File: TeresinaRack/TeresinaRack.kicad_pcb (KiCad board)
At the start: 12 copper layers, 68 x 40 mm, 209 parts, among them J3 USB_Micro-B, J4 SWD, J5 PATCH_SM_EDGE, Q1 MMBT3904, Q2 MMBT3904, SW1 RESET, SW2 BOOT, U1 STM32H750IBK6, U12 TL074, U13 MCP6004, U14 MCP6004, U15 MCP6004, U16 LM4040DBZ-10, U2 IS25LP064A, U3 AS4C16M32MSA-6BIN, U4 PCM3060, U6 TPS62170DSGR, U7 LD1117S50, U8 USBLC6-2SC6, Y1 16MHz

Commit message: Fix via-in-keepout and add bottom-side fiducials
- Move +3V3 edge-feed via (3.18,7.27) out of the F/B keepout zone
- Add FIDB2/FIDB3 (B.Cu) for double-sided assembly vision (3 bottom fiducials)
- U6 PG left unconnected by design (unused open-drain, no pull-up needed)
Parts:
- added FIDB2: Fiducial_1mm_Mask2mm, Fiducial_1mm_Mask2mm, B.Cu at (58.0, 30.4)
- added FIDB3: Fiducial_1mm_Mask2mm, Fiducial_1mm_Mask2mm, B.Cu at (49.9, 11.4)
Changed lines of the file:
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@@
 		)
 	)
+	(footprint "Fiducial_1mm_Mask2mm"
+		(layer "B.Cu")
+		(at 49.9 11.4 180)
+		(descr "Fiducial, circular marking, 1mm bare copper, 2mm soldermask opening (Level A)")
+		(tags "fiducial")
+		(property "Reference" "FIDB3"
+			(at 0 1.95 0)
+			(layer "B.SilkS")
+			(effects
+				(font
+					(size 1 1)
+					(thickness 0.15)
+				)
+				(justify mirror)
+			)
+		)
+		(property "Value" "Fiducial_1mm_Mask2mm"
+			(at 0 -1.95 0)
+			(layer "B.Fab")
+			(effects
+				(font
+					(size 1 1)
+					(thickness 0.15)
+				)
+				(justify mirror)
+			)
+		)
+		(property "Datasheet" ""
+			(at 0 0 0)
+			(layer "B.Fab")
+			(hide yes)
+			(effects
+				(font
+					(size 1.27 1.27)
+				)
+				(justify mirror)
+			)
+		)
+		(property "Description" ""
+			(at 0 0 0)
+			(layer "B.Fab")
+			(hide yes)
+			(effects
+				(font
+					(size 1.27 1.27)
+				)
+				(justify mirror)
+			)
+		)
+		(property "KiLib_Generator" "fiducial"
+			(at 0 0 0)
+			(layer "B.SilkS")
+			(hide yes)
+			(effects
+				(font
+					(size 1 1)
+					(thickness 0.15)
+				)
+				(justify mirror)
+			)
+		)
+		(attr smd exclude_from_pos_files exclude_from_bom)
+		(duplicate_pad_numbers_are_jumpers no)
+		(fp_circle
+			(center 0 0)
+			(end 1.25 0)
+			(stroke
+				(width 0.05)
+				(type solid)
+			)
+			(fill no)
+			(layer "B.CrtYd")
+		)
+		(fp_circle
+			(center 0 0)
+			(end 1 0)
+			(stroke
+				(width 0.1)
+				(type solid)
+			)
+			(fill no)
+			(layer "B.Fab")
+		)
+		(fp_text user "${REFERENCE}"
+			(at 0 0 0)
+			(layer "B.Fab")
+			(effects
+				(font
+					(size 0.5 0.5)
+					(thickness 0.08)
+				)
+				(justify mirror)
+			)
+		)
+		(pad "" smd circle
+			(at 0 0 180)
+			(size 1 1)
+			(layers "B.Cu" "B.Mask")
+			(net "GND")
+			(solder_mask_margin 0.5)
+			(clearance 0.6)
+		)
+		(embedded_fonts no)
+	)
 	(footprint "Capacitor_SMD:C_0402_1005Metric"
 		(layer "B.Cu")
@@
 		)
 	)
+	(footprint "Fiducial_1mm_Mask2mm"
+		(layer "B.Cu")
+		(at 58 30.4 180)
+		(descr "Fiducial, circular marking, 1mm bare copper, 2mm soldermask opening (Level A)")
+		(tags "fiducial")
+		(property "Reference" "FIDB2"
+			(at 0 1.95 0)
+			(layer "B.SilkS")
+			(effects
+				(font
+					(size 1 1)
+					(thickness 0.15)
+				)
+				(justify mirror)
+			)
+		)
+		(property "Value" "Fiducial_1mm_Mask2mm"
+			(at 0 -1.95 0)
+			(layer "B.Fab")
+			(effects
+				(font
+					(size 1 1)
+					(thickness 0.15)
+				)
+				(justify mirror)
+			)
+		)
+		(property "Datasheet" ""
+			(at 0 0 0)
+			(layer "B.Fab")
+			(hide yes)
+			(effects
+				(font
+					(size 1.27 1.27)
+				)
+				(justify mirror)
+			)
+		)
+		(property "Description" ""
+			(at 0 0 0)
+			(layer "B.Fab")
+			(hide yes)
+			(effects
+				(font
+					(size 1.27 1.27)
+				)
+				(justify mirror)
+			)
+		)
+		(property "KiLib_Generator" "fiducial"
+			(at 0 0 0)
+			(layer "B.SilkS")
+			(hide yes)
+			(effects
+				(font
+					(size 1 1)
+					(thickness 0.15)
+				)
+				(justify mirror)
+			)
+		)
+		(attr smd exclude_from_pos_files exclude_from_bom)
+		(duplicate_pad_numbers_are_jumpers no)
+		(fp_circle
+			(center 0 0)
+			(end 1.25 0)
+			(stroke
+				(width 0.05)
+				(type solid)
+			)
+			(fill no)
+			(layer "B.CrtYd")
+		)
+		(fp_circle
+			(center 0 0)
+			(end 1 0)
+			(stroke
+				(width 0.1)
+				(type solid)
+			)
+			(fill no)
+			(layer "B.Fab")
+		)
+		(fp_text user "${REFERENCE}"
+			(at 0 0 0)
+			(layer "B.Fab")
+			(effects
+				(font
+					(size 0.5 0.5)
+					(thickness 0.08)
+				)
+				(justify mirror)
+			)
+		)
+		(pad "" smd circle
+			(at 0 0 180)
+			(size 1 1)
+			(layers "B.Cu" "B.Mask")
+			(net "GND")
+			(solder_mask_margin 0.5)
+			(clearance 0.6)
+		)
+		(embedded_fonts no)
+	)
 	(footprint "Capacitor_SMD:C_0402_1005Metric"
 		(layer "B.Cu")
@@
 	(segment
 		(start 1.92 7.27)
-		(end 3.1798 7.27)
+		(end 2.7 7.27)
 		(width 0.2)
 		(layer "F.Cu")
@@
 	)
 	(via
-		(at 3.1798 7.27)
+		(at 2.7 7.27)
 		(size 0.3)
 		(drill 0.15)

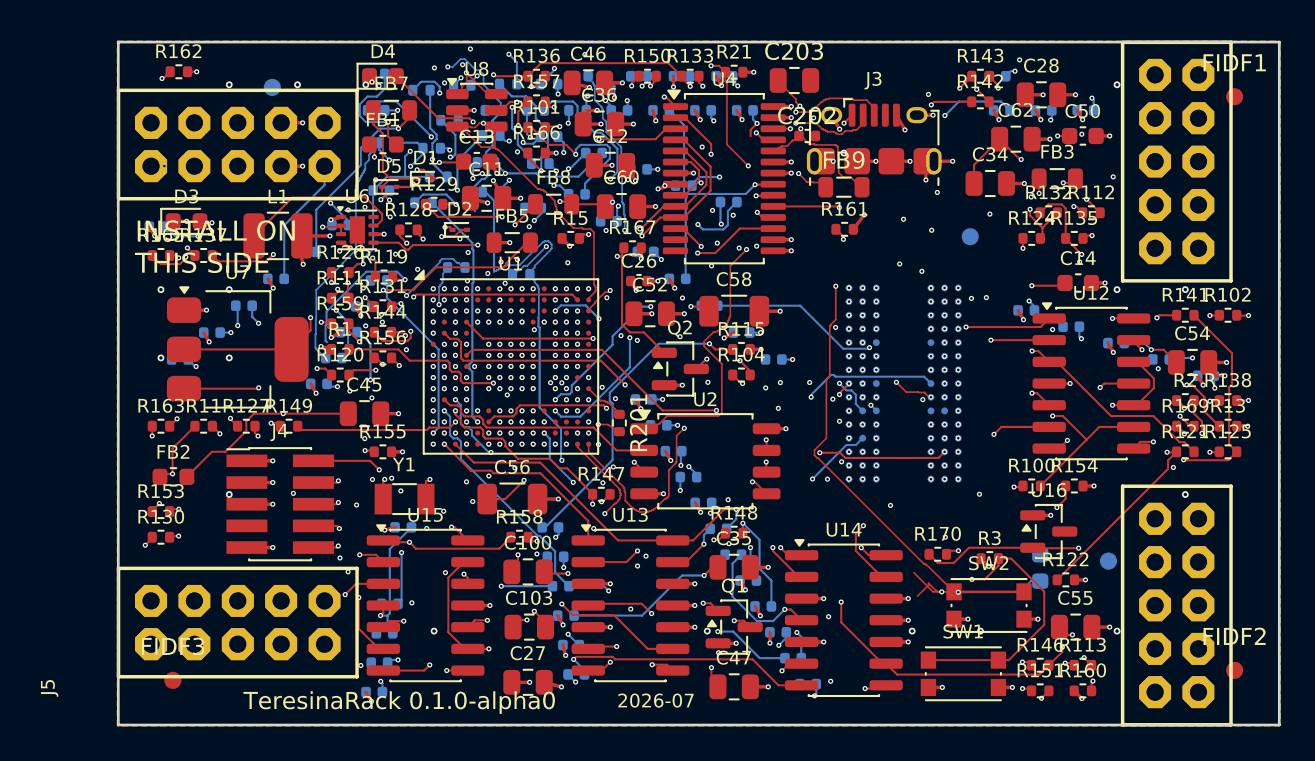
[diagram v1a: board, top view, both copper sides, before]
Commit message: Resolve codec-supply/J3 collision: relocate +5VA parts, route via analog corridor
- FB9/C202/C203 were inside the J3 micro-USB body (FB9 2.1mm2, C202 0.41mm2 overlap)
- Relocate to B.Cu: C202 (100nF) in the clear pocket under U4.24; FB9+C203 by the
  analog +5V rail. Route +5VA up the analog corridor (from U14 area) to a via-in-pad
  at U4.24 - avoids the saturated inter-BGA band. 0mm2 J3-body overlap now.
- Revert the +3V3 edge via to its original spot (KiCad DRC has no keepout error there;
  the earlier move created a real hole-to-hole vs J5.A10). Drop FIDB3 (no clear spot).
- DRC: 0 shorts / 0 clearance / 0 hole / 0 unconnected. Only pre-existing R201 courtyard.
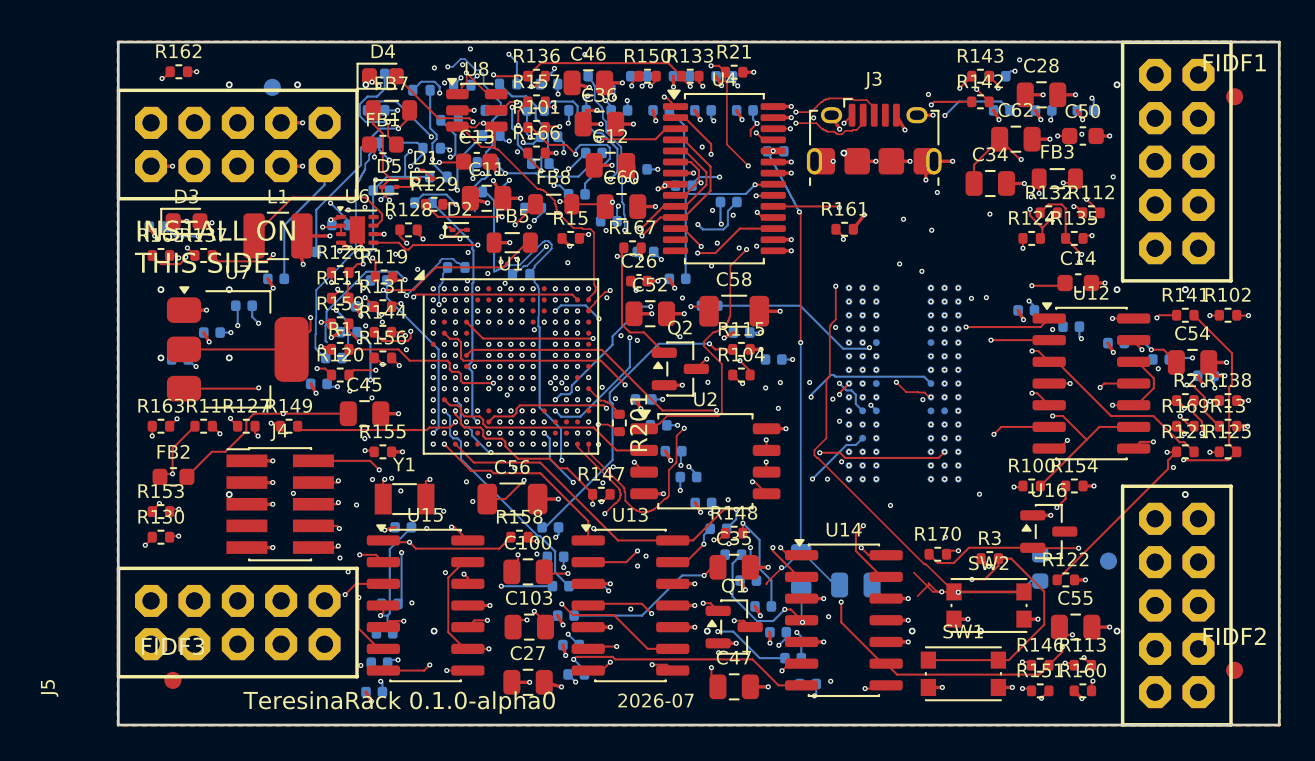
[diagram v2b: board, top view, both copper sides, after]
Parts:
- removed FIDB3: Fiducial_1mm_Mask2mm, Fiducial_1mm_Mask2mm
- C202, C203, FB9: moved to B.Cu
- moved C203 29.8 mm to (43.2, 31.8)
- moved FB9 22.5 mm to (40.0, 30.9), turned to 90 degrees
- moved C202 2.06 mm to (38.5, 6.40)
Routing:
- net +5VA: track 11.2 -> 29.9 mm, vias 2 -> 4
